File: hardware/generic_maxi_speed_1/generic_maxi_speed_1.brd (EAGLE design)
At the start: 50 x 50 mm, 31 parts, among them IC1 MEGA48/88/168-PU, IC2 RFM12, IC3 LP2950Z, Q1 20MHz

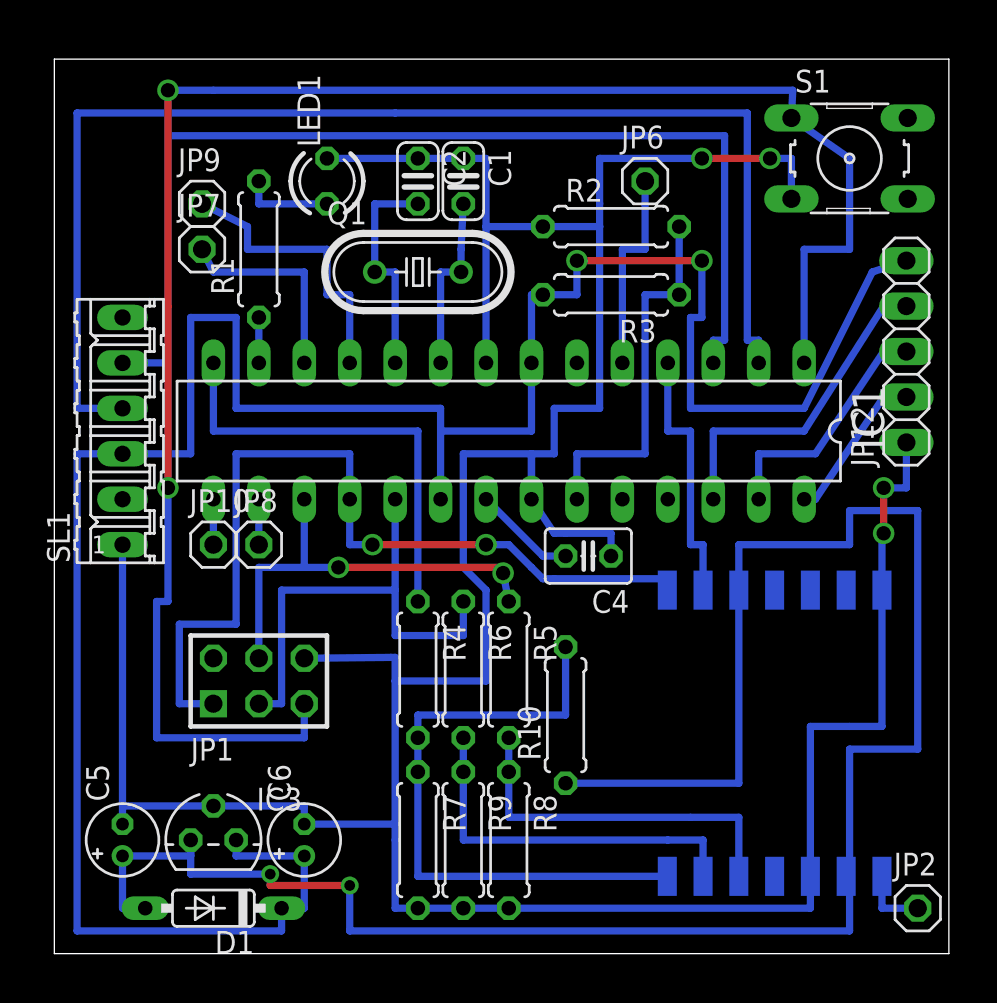
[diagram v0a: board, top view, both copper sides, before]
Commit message: Moved capacitor near to RFM12. Added zener diodes instead of resistors. Avoid one bridge connection.
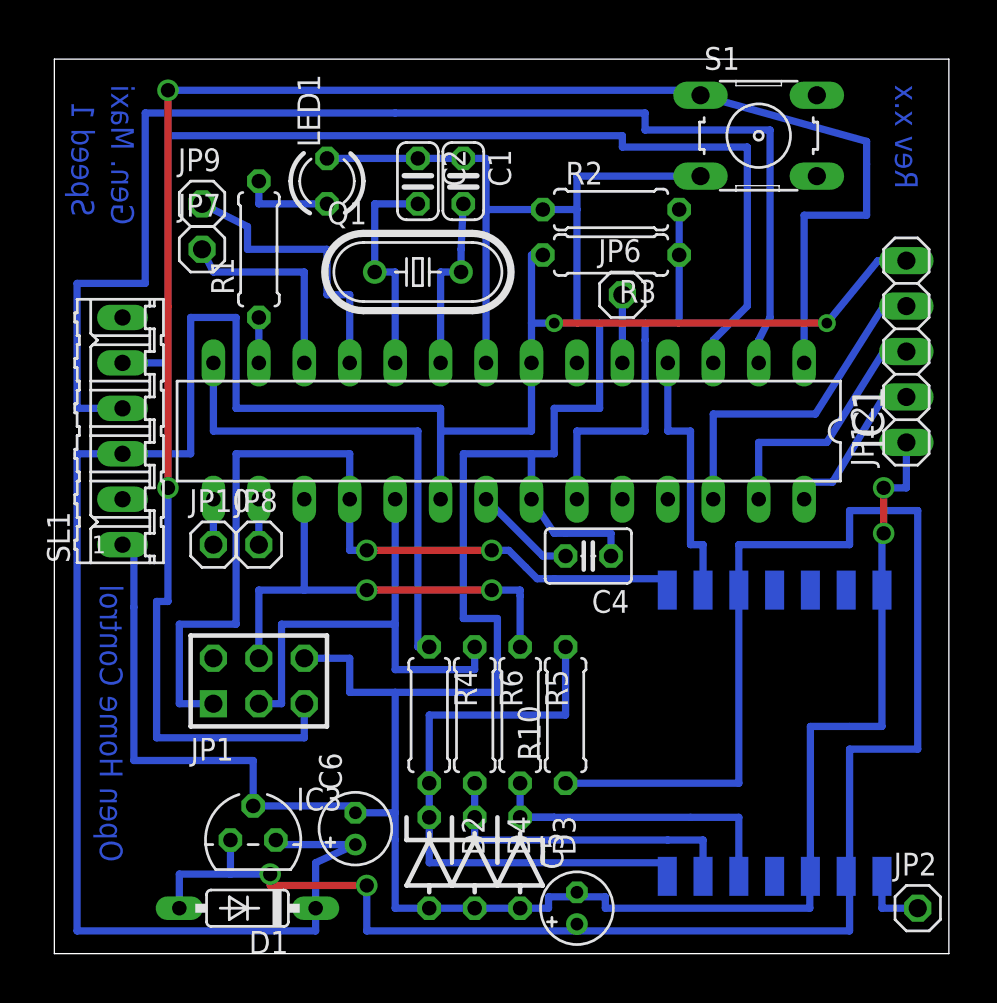
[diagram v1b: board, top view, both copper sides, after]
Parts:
- removed R7, R8, R9: 3k3, rcl:0207/7
- added D2, D3, D4: 3.3V, diode:ZDIO-5
- JP12: value (none) -> FEATURE
- R4, R5, R6: value 1k8 -> 1k
- moved C5 25.7 mm to (29.2, 2.54)
- moved JP6 6.48 mm to (31.8, 36.8)
- moved S1 5.24 mm to (39.4, 45.7)
- moved C6 2.93 mm to (16.8, 6.99)
- moved R5 2.62 mm to (26.0, 13.3)
- moved R6 2.62 mm to (23.5, 13.3)
- moved R4 2.62 mm to (21.0, 13.3)
- moved R3 2.22 mm to (31.1, 39.1)
- moved IC3 2.22 mm to (11.1, 6.35)
- moved D1 1.90 mm to (10.8, 2.54)
- moved R2 0.95 mm to (31.1, 41.6)
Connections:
- net GND: now also D2.A, D3.A, D4.A; no longer R7.2, R8.2, R9.2
- net N$16: now also D3.C; no longer R8.1
- net N$27: now also D2.C; no longer R7.1
- net N$5: now also D4.C; no longer R9.1
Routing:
- net +5V: track 136.3 -> 127.2 mm
- net N$17: track 11.4 -> 3.81 mm
- net +3V3: track 113.4 -> 107.8 mm
- net GND: track 199.4 -> 194.9 mm, vias 4 -> 2
- net N$5: track 21.1 -> 18.0 mm
- net N$26: track 24.8 -> 27.9 mm
- net N$3: track 24.5 -> 26.7 mm
- net N$9: track 59.7 -> 61.1 mm
- net N$16: track 20.6 -> 19.3 mm
- net N$27: track 35.0 -> 33.8 mm
- net N$8: track 101.4 -> 102.4 mm
- net N$18: track 21.0 -> 21.9 mm
- net N$10: track 71.1 -> 71.9 mm
- net N$6: track 8.77 -> 9.36 mm
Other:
- board text added: "Gen. Maxi"
- board text added: "Open Home Control"
- board text added: "Rev x.x"
- board text added: "Speed 1"
